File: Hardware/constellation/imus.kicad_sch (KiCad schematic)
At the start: 5 parts, among them U2 ICM-45686, U3 LSM6DSL

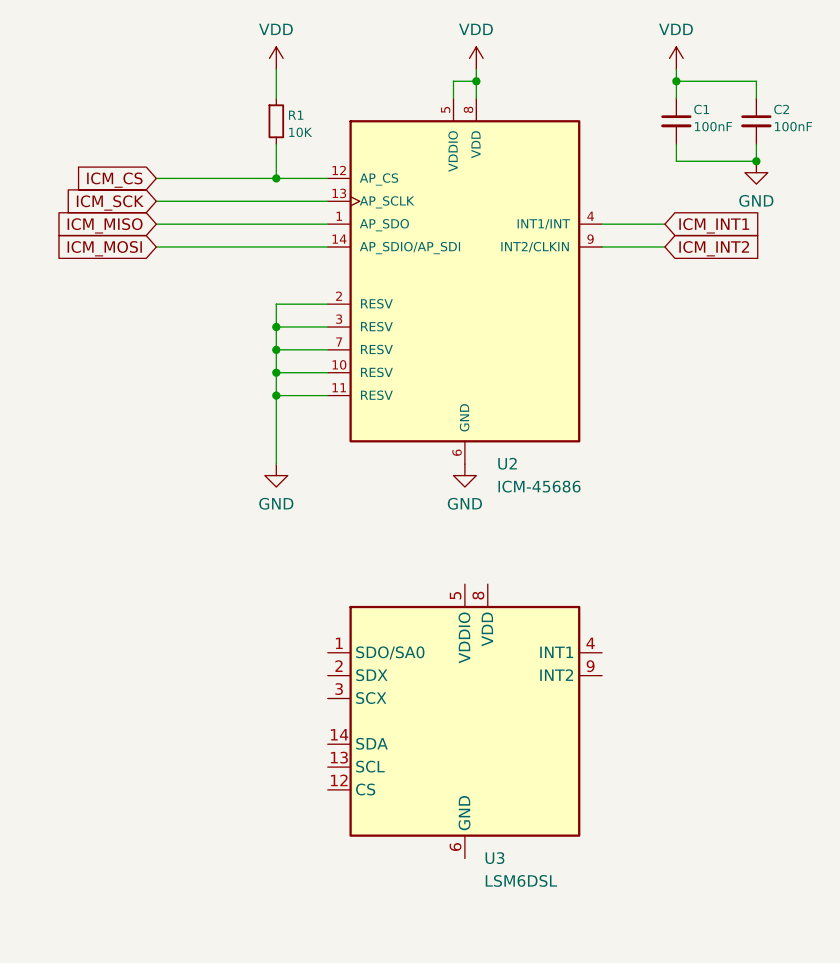
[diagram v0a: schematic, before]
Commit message: add baro sheet and finalize imus
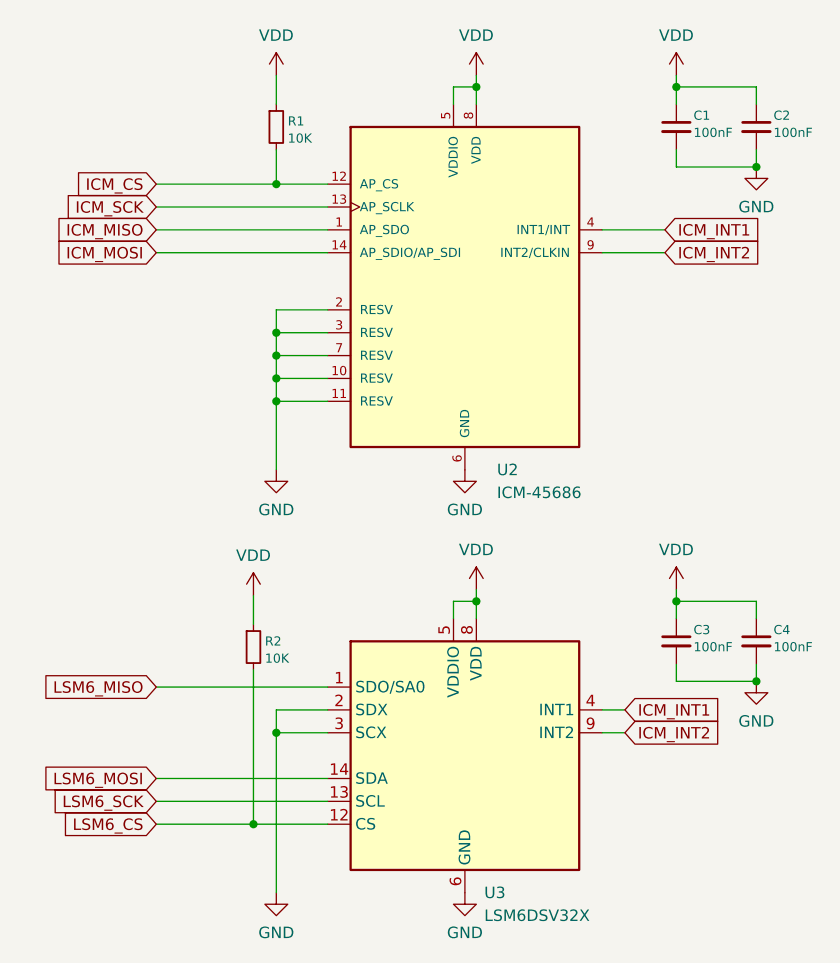
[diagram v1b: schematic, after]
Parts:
- added C3, C4: 100nF, Capacitor_SMD:C_0402_1005Metric, symbol Device:C_Small
- added R2: 10K, Resistor_SMD:R_0402_1005Metric_Pad0.72x0.64mm_HandSolder, symbol Device:R_Small
- U3: value LSM6DSL -> LSM6DSV32X
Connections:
- net GND: now also U3.2 (SDX), U3.3 (SCX), U3.6 (GND), U3.7 (GND), C3.2, C4.2
- net ICM_INT1: now also U3.4 (INT1)
- net ICM_INT2: now also U3.9 (INT2)
- net VDD: now also U3.5 (VDDIO), U3.8 (VDD), C3.1, C4.1, R2.1
- net LSM6_MISO: now reaches U3.1 (SDO/SA0)
- net LSM6_CS: now reaches U3.12 (CS)
- net LSM6_CS: now also R2.2
- net LSM6_SCK: now reaches U3.13 (SCL)
- net LSM6_MOSI: now reaches U3.14 (SDA)
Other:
- moved on the sheet: C1, C2, R1, U2, U3
